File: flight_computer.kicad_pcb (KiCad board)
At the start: 4 copper layers, 95.9 x 90.2 mm, 158 parts, among them J1 436500204, J10 TSW-102-07-F-S, J11 TSW-103-07-F-S, J12 SMA-J-P-H-ST-EM1, J2 0530480210, J3 0530480210, J4 398800302, J5 398800302, J6 398800302, J7 398800302, J8 0530480810, J9 USB4105-GF-A-120, Q6 SI1016CX-T1-GE3, Q7 DMT6007LFGQ-7, U1 LQFP100, U10 LT6000IDCB#TRMPBF, U11 NC7WZ07P6X, U12 B39162B4300F210, U13 MS561101BA03-50, U14 IAM-20380HT, U15 H3LIS331DLTR, U16 LM74700QDRQ1, U2 INA229AQDGSRQ1, U3 TPS62130AQRGTRQ1, U4 TPS62130AQRGTRQ1, U5 S25FL256LAGNFM010, U6 SOT-666-6, U7 MMC5983MA, U8 AIS2IHTR, U9 MAX-M10S-00B, Y1 25MHz

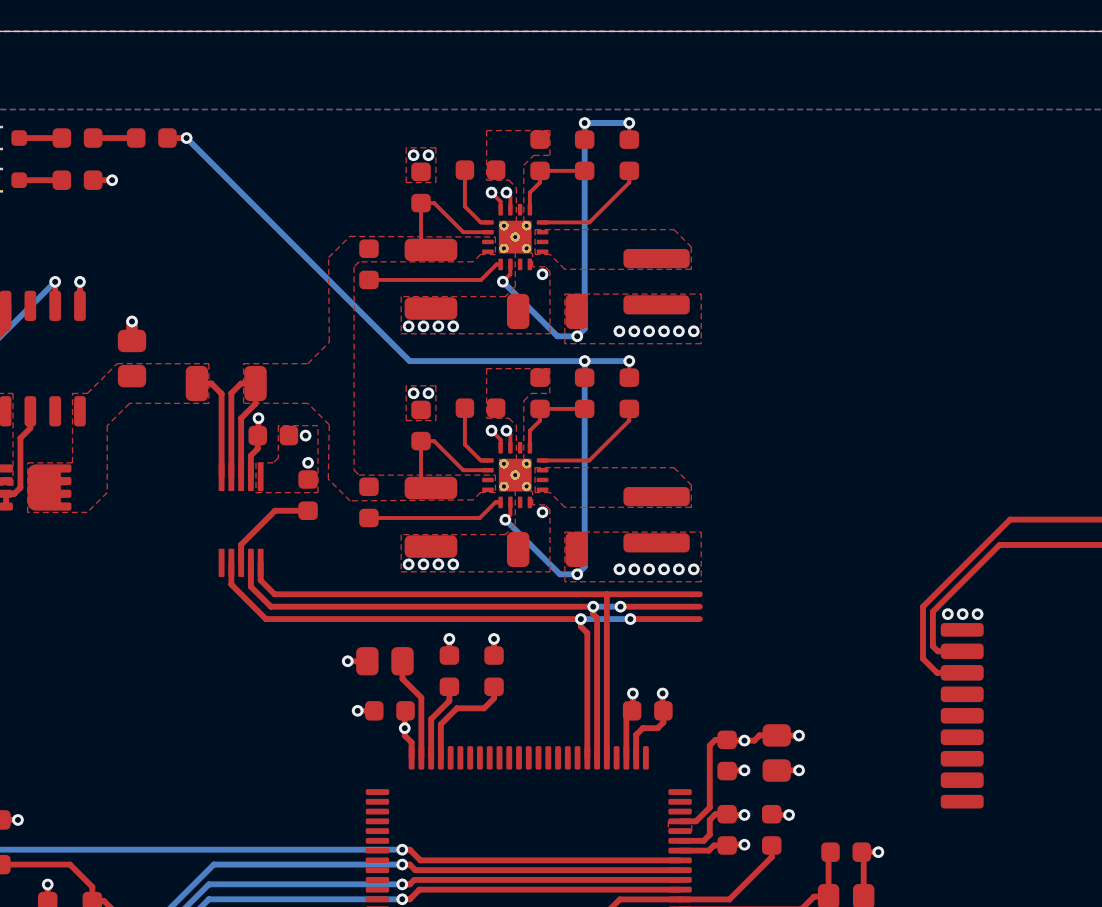
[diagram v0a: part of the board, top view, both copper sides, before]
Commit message: - On push in main create a new set of documents - On release fix images - Update README to use correct images
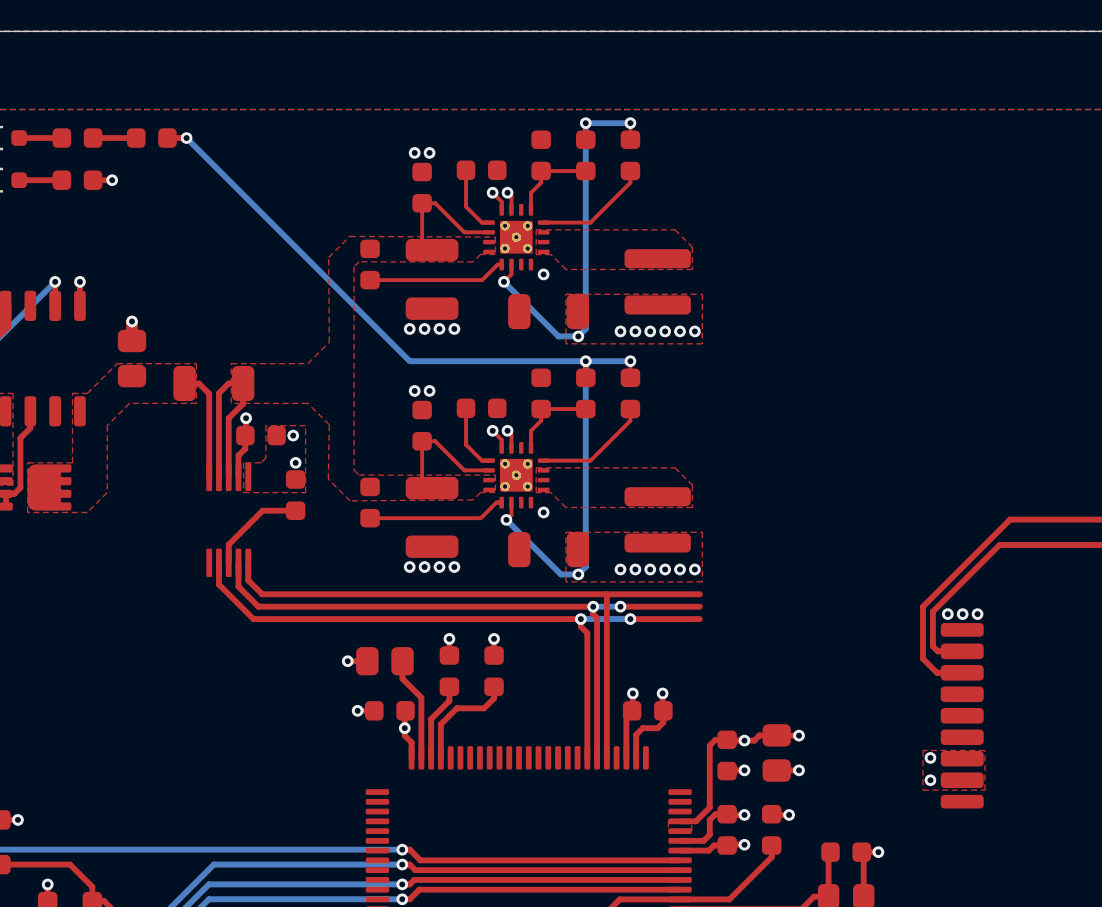
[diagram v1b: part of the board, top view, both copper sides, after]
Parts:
- moved C4 0.63 mm to (139.0, 71.2)
- moved R4 0.63 mm to (136.6, 68.6)
- moved R5 0.63 mm to (140.8, 74.3)
- moved U2 0.63 mm to (137.3, 75.5)
- moved C19 0.06 mm to (150.3, 57.6)
- moved C20 0.06 mm to (150.3, 69.8)
- moved C23 0.06 mm to (153.7, 64.9)
- moved R18 0.06 mm to (153.3, 56.9)
- moved R20 0.06 mm to (153.3, 69.1)
- moved C24 0.06 mm to (153.7, 77.1)
- moved C18 0.06 mm to (147.2, 70.7)
- moved L2 0.06 mm to (159.3, 75.5)
- moved R13 0.06 mm to (157.9, 56.9)
- moved R14 0.06 mm to (157.9, 69.1)
- moved R17 0.06 mm to (155.6, 56.9)
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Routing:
- net SPI1.SCLK: track 32.1 -> 32.7 mm
- net SPI1.MOSI: track 33.1 -> 33.7 mm
- net SPI1.MISO: track 32.5 -> 33.1 mm
- net +3.3V: vias 36 -> 38

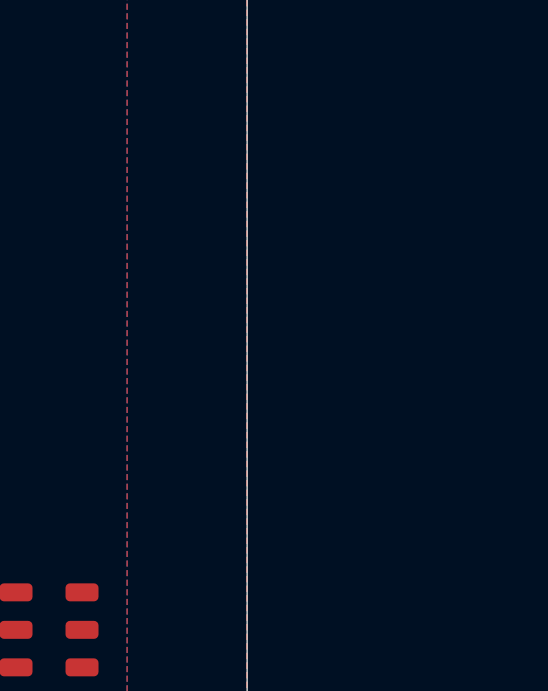
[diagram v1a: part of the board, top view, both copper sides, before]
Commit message: Major fix: move from a flat to a hierarchical architecture for schematic.
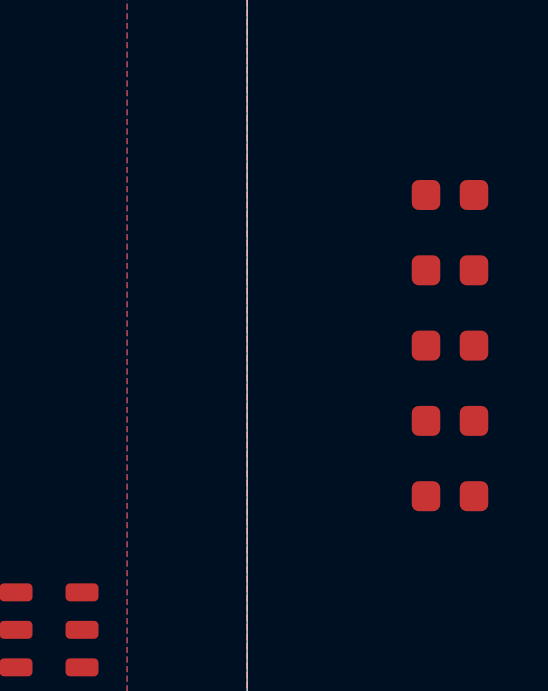
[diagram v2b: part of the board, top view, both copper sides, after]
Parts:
- added R54: 10kΩ, passive_resistor:R_0603_Density_Nominal, F.Cu at (207.3, 103.7)
- added R55: 10kΩ, passive_resistor:R_0603_Density_Nominal, F.Cu at (207.3, 106.2)
- added R56: 10kΩ, passive_resistor:R_0603_Density_Nominal, F.Cu at (207.3, 108.8)
- added R57: 10kΩ, passive_resistor:R_0603_Density_Nominal, F.Cu at (207.3, 111.3)
- added R58: 10kΩ, passive_resistor:R_0603_Density_Nominal, F.Cu at (207.3, 113.8)
- U1: value LQFP100 -> STM32F405VGT7
- U6: value SOT-666-6 -> USBLC6-2P6
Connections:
- net /mcu/BOOT0 renamed /Microcontroller/BOOT0
- net /mcu/CAN2.RX renamed /Microcontroller/CAN2.RX
- net /mcu/CAN2.TX renamed /Microcontroller/CAN2.TX
- net /mcu/CC1 renamed /Microcontroller/CC1
- net /mcu/CC2 renamed /Microcontroller/CC2
- net /mcu/RCC_OSC_IN renamed /Microcontroller/RCC_OSC_IN
- net /mcu/RCC_OSC_OUT renamed /Microcontroller/RCC_OSC_OUT
- net /mcu/USB_CONN_D+ renamed /Microcontroller/USB_CONN_D+
- net /mcu/USB_CONN_D- renamed /Microcontroller/USB_CONN_D-
- net /mcu/V_CAP1 renamed /Microcontroller/V_CAP1
- net /mcu/V_CAP2 renamed /Microcontroller/V_CAP2
- net /power/+3.3V_EN renamed /Power/+3.3V_EN
- net /power/+3.3V_FB renamed /Power/+3.3V_FB
- net /power/+3.3V_PG renamed /Power/+3.3V_PG
- net /power/+3.3V_SS/TR renamed /Power/+3.3V_SS/TR
- net /power/+3.3V_SW renamed /Power/+3.3V_SW
- net /power/+5V_EN renamed /Power/+5V_EN
- net /power/+5V_FB renamed /Power/+5V_FB
- net /power/+5V_PG renamed /Power/+5V_PG
- net /power/+5V_SS/TR renamed /Power/+5V_SS/TR
- net /power/+5V_SW renamed /Power/+5V_SW
- net /power/VCAP renamed /Power/VCAP
- net /power/VIN_PROT renamed /Power/VIN_PROT
- net /power/VSENSE renamed /Power/VSENSE
- net /rf/ANT_DETECT renamed /RF/ANT_DETECT
- net /rf/ANT_SHORT renamed /RF/ANT_SHORT
- net /rf/LNA_EN renamed /RF/LNA_EN
- net /rf/RF_IN renamed /RF/RF_IN
- net /sensors/GYRO_REGOUT renamed /Sensors/GYRO_REGOUT
- net /sensors/MAG_CAP renamed /Sensors/MAG_CAP

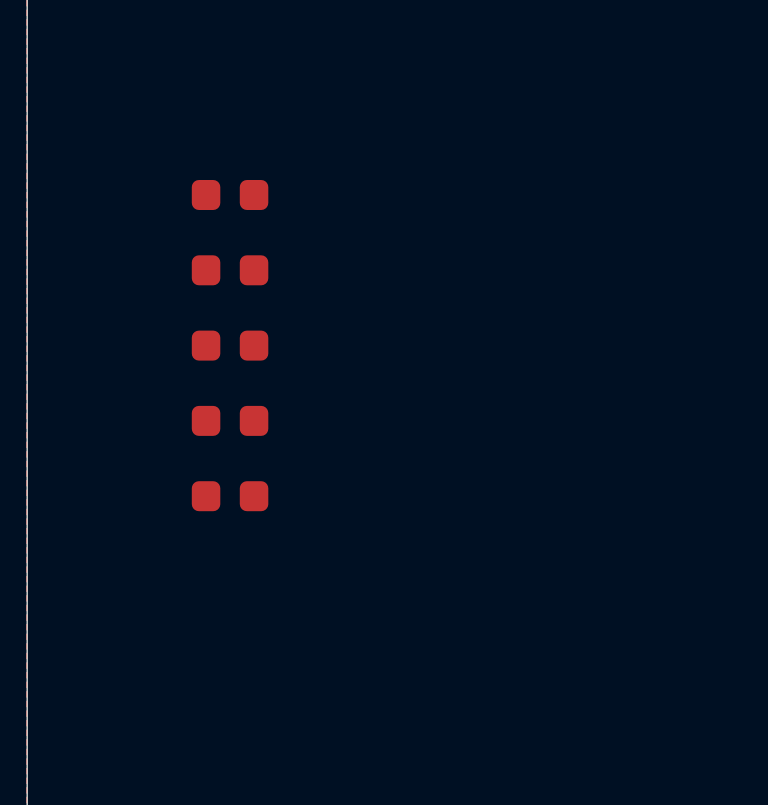
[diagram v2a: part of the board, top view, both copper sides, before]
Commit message: Added measurements to PCB view
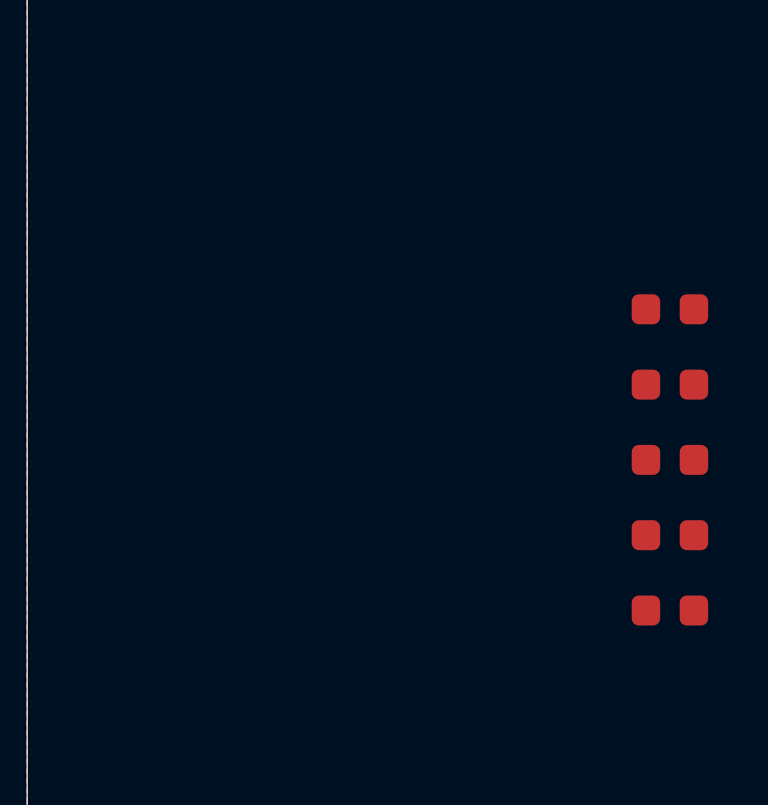
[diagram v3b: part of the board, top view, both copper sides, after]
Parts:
- moved R54 15.1 mm to (222.0, 107.5)
- moved R55 15.1 mm to (222.0, 110.0)
- moved R56 15.1 mm to (222.0, 112.6)
- moved R58 15.1 mm to (222.0, 117.6)
- moved R57 15.1 mm to (222.0, 115.1)
